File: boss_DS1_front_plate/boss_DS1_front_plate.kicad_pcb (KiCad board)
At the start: 2 copper layers, 80 x 100 mm, 13 parts, among them J1 top_panel_connector

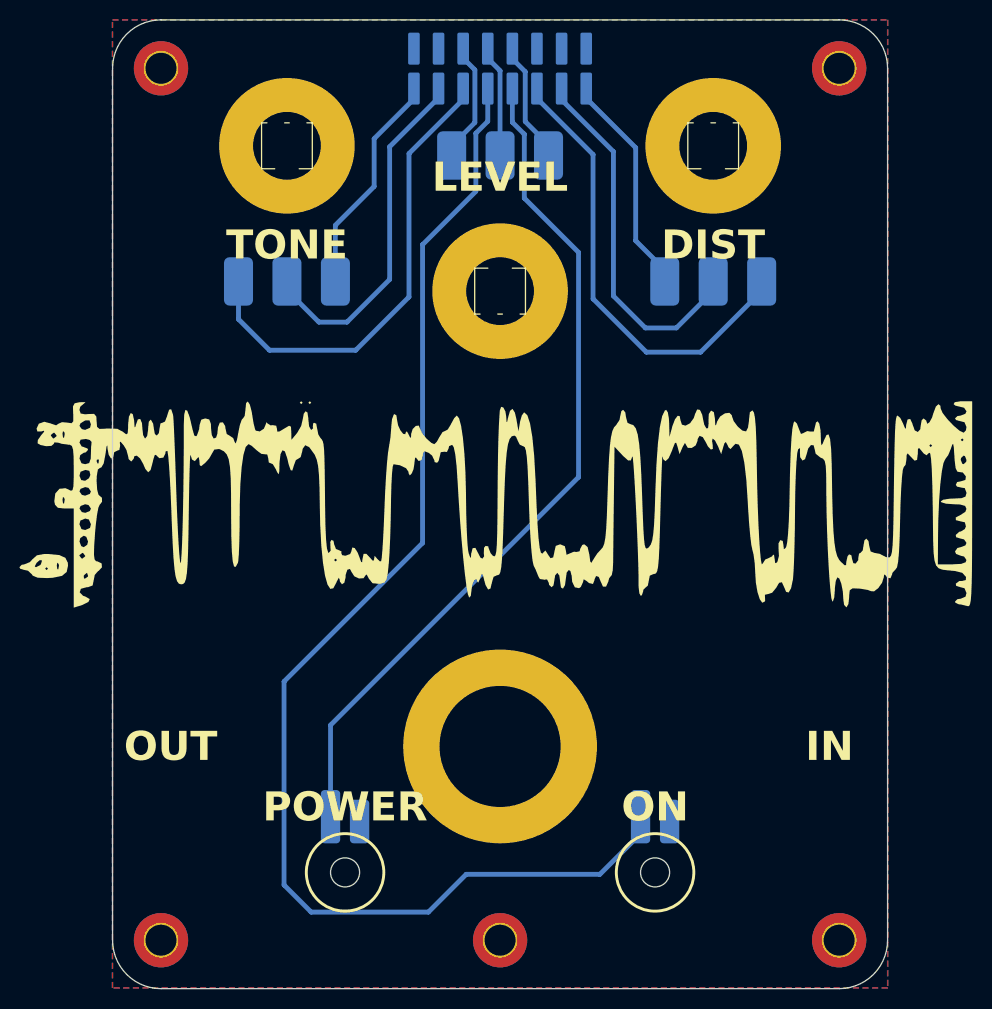
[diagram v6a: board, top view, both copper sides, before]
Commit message: Top plate rounded.
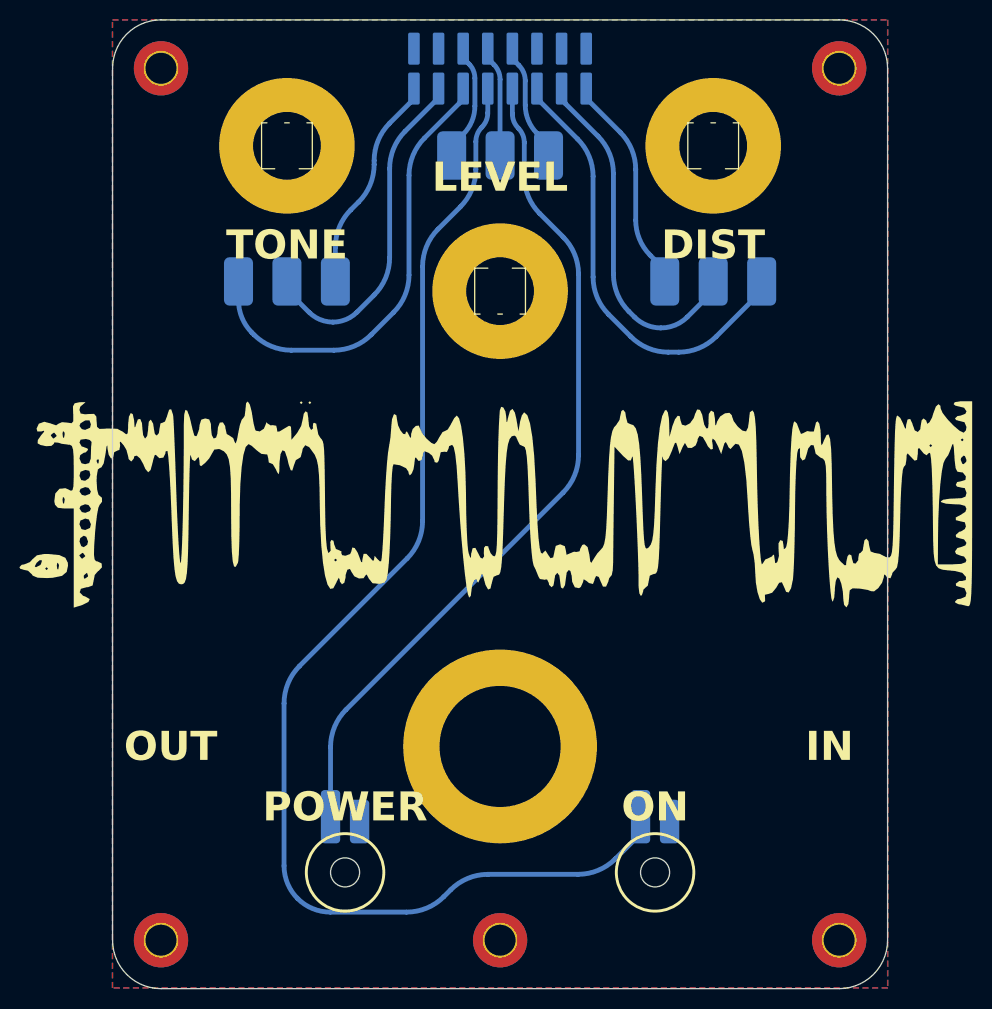
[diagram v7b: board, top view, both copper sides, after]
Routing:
- net Net-(D1-A): track 134.0 -> 131.4 mm
- net Net-(J1A-Pin_6): track 49.9 -> 47.6 mm
- net Net-(D2-A): track 88.6 -> 87.3 mm
- net Net-(J1C-Pin_12): track 47.4 -> 46.2 mm
- net Net-(J1C-Pin_14): track 37.9 -> 36.8 mm
- net Net-(J1A-Pin_4): track 36.5 -> 35.5 mm
- net Net-(J1A-Pin_2): track 23.3 -> 22.4 mm
- net Net-(J1C-Pin_16): track 23.3 -> 22.6 mm
